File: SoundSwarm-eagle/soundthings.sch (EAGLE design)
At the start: 32 parts, among them Q2 MOSFET-NCHANNEL2N7000, Q4 MOSFET-NCHANNEL2N7000, Q5 MOSFET-PCHANNELFQP27P06

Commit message: v2 (to be tested)
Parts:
- added R13: 300, SparkFun-Passives:RESISTORAXIAL-0.3
- D1: value (none) -> 1N4001
- D3: value DIODE-ZENERPTH -> 1N5817; device SparkFun-DiscreteSemi:DIODE-ZENERPTH -> adafruit:SCHOTTKY-DIODEDO41
- Q1: value MOSFET-PCHANNELFQP27P06 -> IRLIB9343PbF
- Q2, Q4: value MOSFET-NCHANNEL2N7000 -> IRLB8721PBF; device SparkFun-DiscreteSemi:MOSFET-NCHANNEL2N7000 -> SparkFun-DiscreteSemi:MOSFET-NCHANNELFQP30N06L
- R8: value (none) -> 300
- U$2: value TP4057SOT-26-R -> TP4057
- renumbered D2 to LED, JP1-3V3 to 3V3, JP1-SOL to SOLENOID, JP2-ADXL to ADXL, JP2-BAT to BAT, Q5 to Q1
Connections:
- net N$10 renamed 5V
- net N$13 renamed GATE
- net N$17 renamed ADC
- net N$4 renamed GPIO16
- new net N$4: C1.-, Q1.D, Q4.D, R13.2
- net N$12: now also R13.1; no longer C1.-, Q1.S, Q4.D
- net VBAT: now also Q1.S; no longer Q1.D

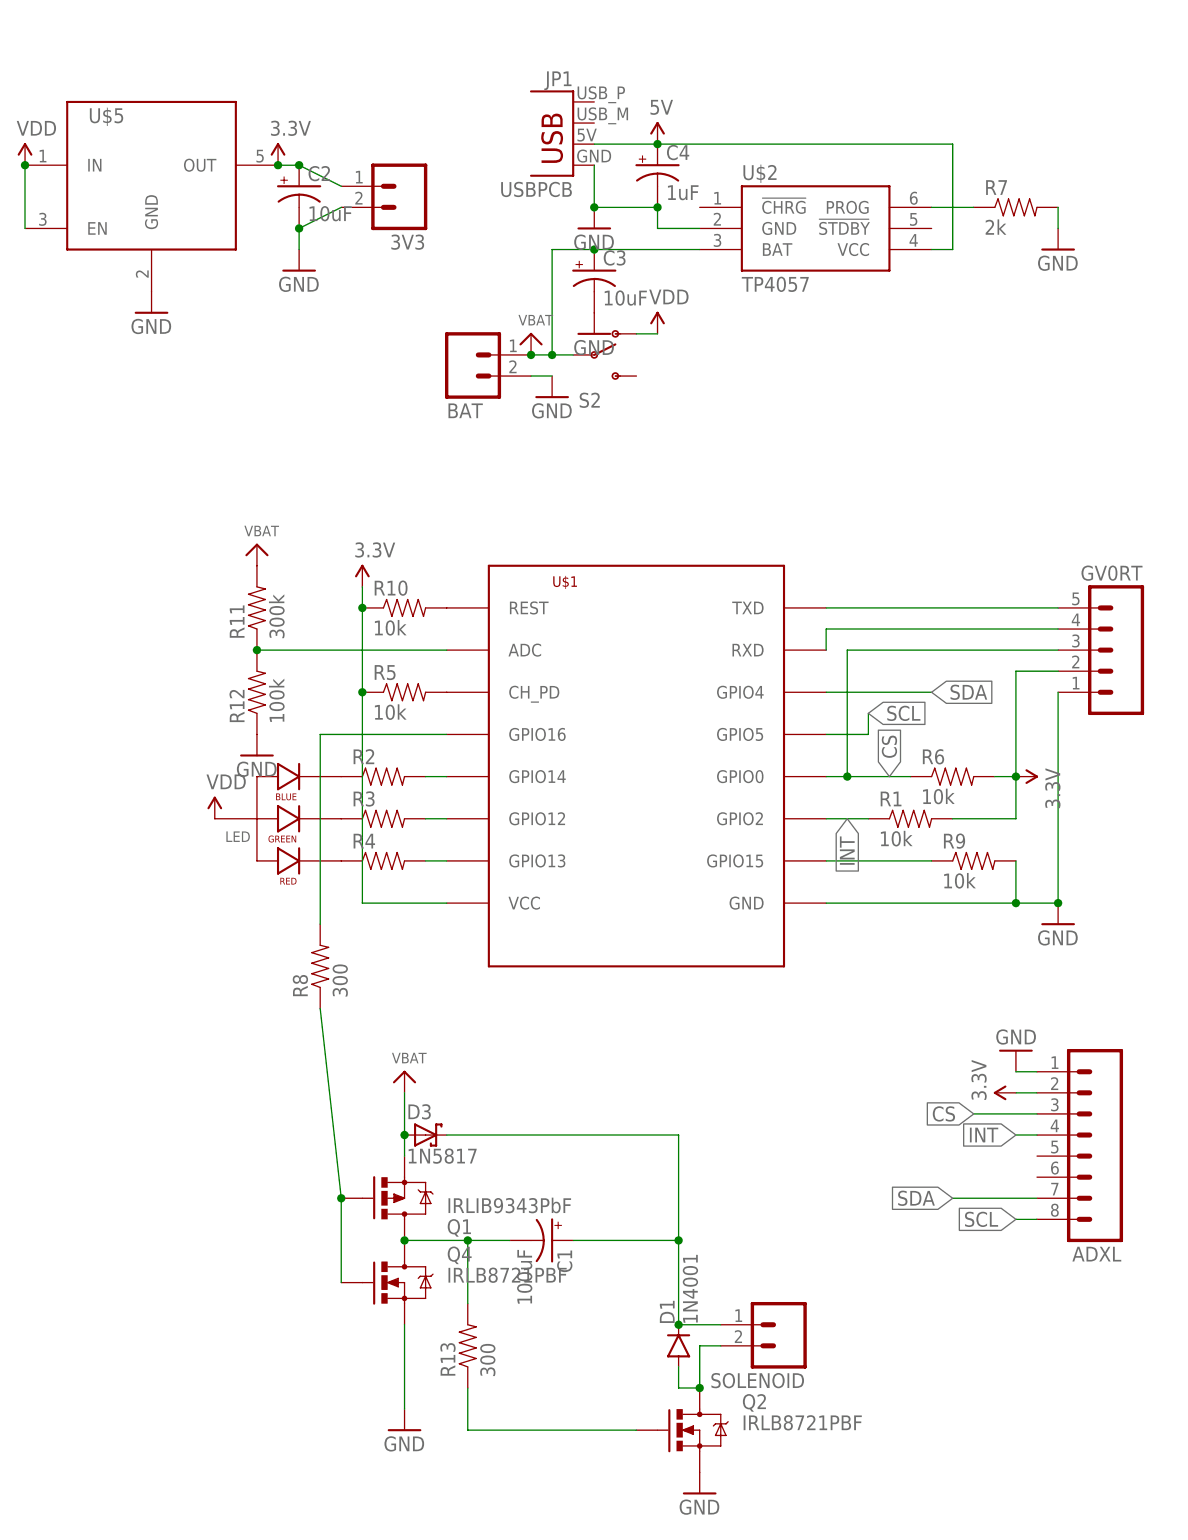
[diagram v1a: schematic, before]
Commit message: Update board with mounting holes
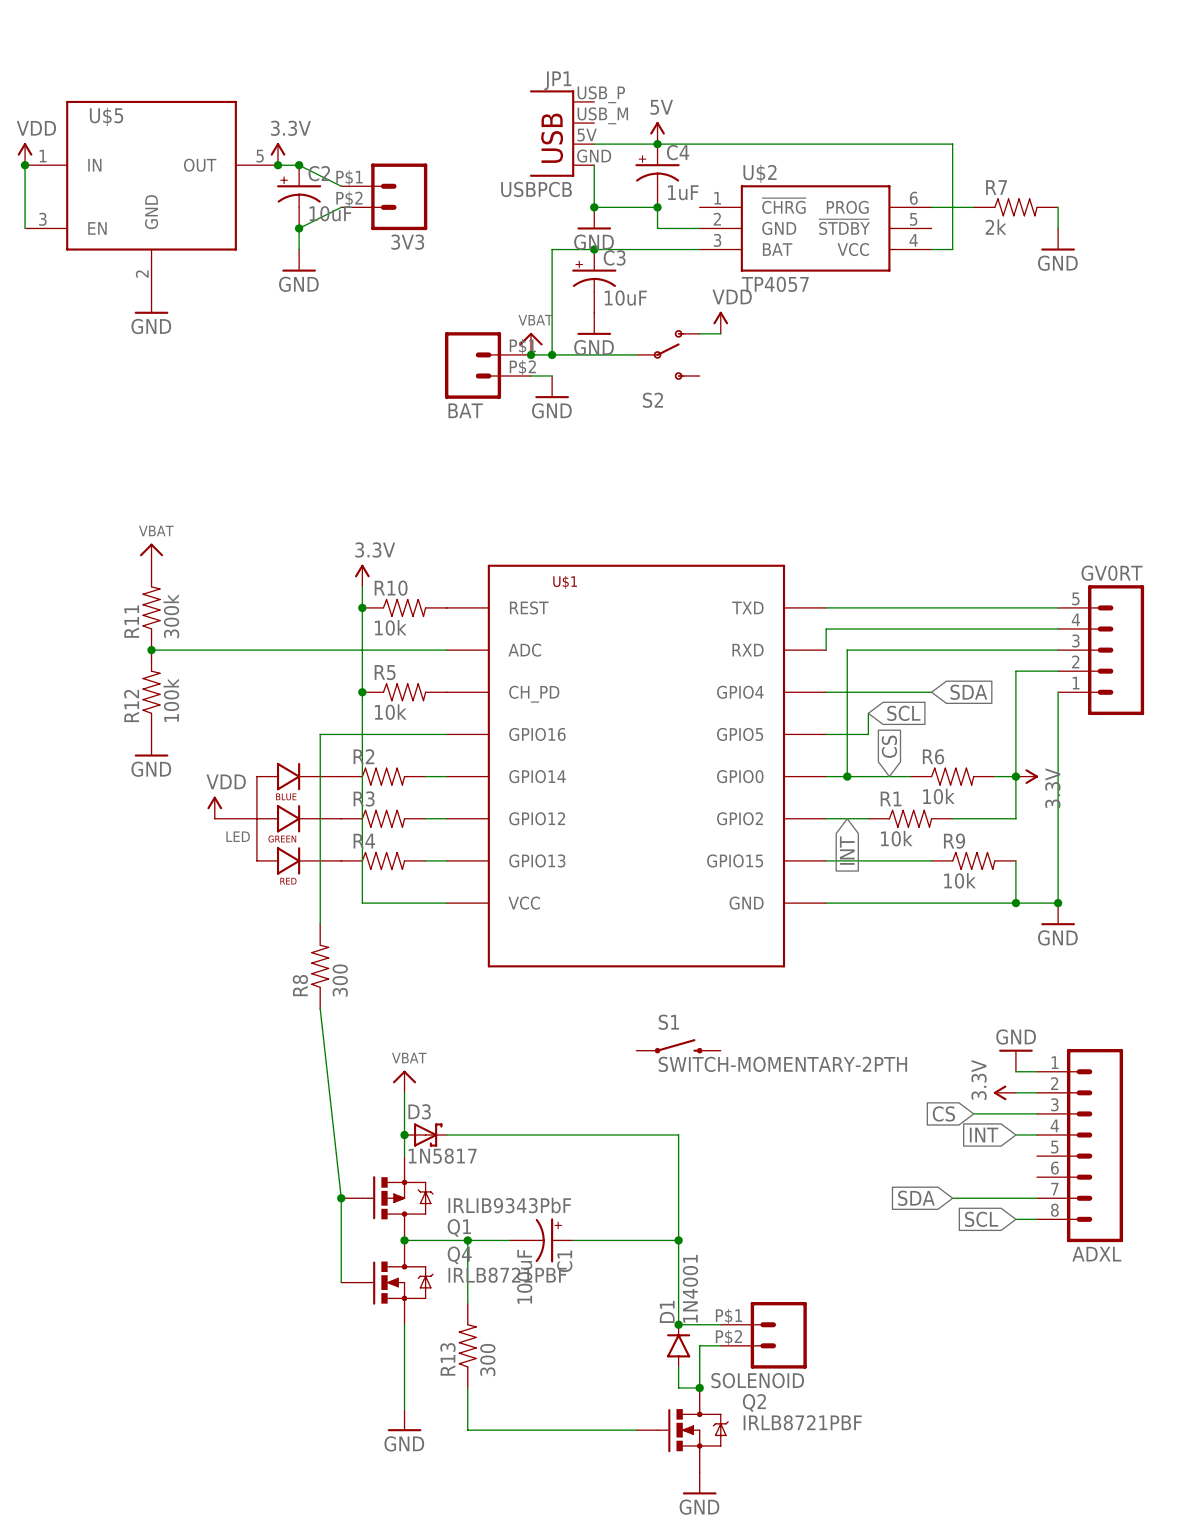
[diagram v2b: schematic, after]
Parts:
- added S1: SWITCH-MOMENTARY-2PTH, SparkFun-Electromechanical:SWITCH-MOMENTARY-2PTH
- 3V3, BAT, SOLENOID: device SparkFun-Connectors:M02JST-PTH-VERT -> SparkFun-Connectors:M02PTH2
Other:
- moved on the sheet: 3V3, BAT, R11, R12, S2, SOLENOID
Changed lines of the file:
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@@
 <part name="U$2" library="lio" deviceset="TP4057" device="SOT-26-R" value="TP4057"/>
 <part name="S2" library="lio" deviceset="SWITCH-SPDT" device="-1"/>
-<part name="SOLENOID" library="SparkFun-Connectors" deviceset="M02" device="JST-PTH-VERT"/>
-<part name="BAT" library="SparkFun-Connectors" deviceset="M02" device="JST-PTH-VERT"/>
+<part name="SOLENOID" library="SparkFun-Connectors" deviceset="M02" device="PTH2"/>
+<part name="BAT" library="SparkFun-Connectors" deviceset="M02" device="PTH2"/>
 <part name="D1" library="SparkFun-DiscreteSemi" deviceset="DIODE" device="1N4148" value="1N4001"/>
 <part name="C1" library="SparkFun-Capacitors" deviceset="100UF-25V-20%(PTH)" device="" value="100uF"/>
@@
 <part name="GND3" library="SparkFun-Aesthetics" deviceset="GND" device=""/>
 <part name="GND4" library="SparkFun-Aesthetics" deviceset="GND" device=""/>
-<part name="3V3" library="SparkFun-Connectors" deviceset="M02" device="JST-PTH-VERT"/>
+<part name="3V3" library="SparkFun-Connectors" deviceset="M02" device="PTH2"/>
 <part name="R5" library="SparkFun-Passives" deviceset="RESISTOR" device="AXIAL-0.3" value="10k"/>
 <part name="R6" library="SparkFun-Passives" deviceset="RESISTOR" device="AXIAL-0.3" value="10k"/>
@@
 <part name="R13" library="SparkFun-Passives" deviceset="RESISTOR" device="AXIAL-0.3" value="300"/>
 <part name="D3" library="adafruit" deviceset="SCHOTTKY-DIODE" device="DO41" value="1N5817"/>
+<part name="S1" library="SparkFun-Electromechanical" deviceset="SWITCH-MOMENTARY-2" device="PTH"/>
 </parts>
 <sheets>
@@
 <instance part="U$1" gate="G$1" x="60.96" y="93.98"/>
 <instance part="U$2" gate="G$1" x="83.82" y="165.1"/>
-<instance part="S2" gate="1" x="58.42" y="149.86"/>
+<instance part="S2" gate="1" x="66.04" y="149.86"/>
 <instance part="SOLENOID" gate="G$1" x="81.28" y="33.02" rot="R180"/>
 <instance part="BAT" gate="G$1" x="43.18" y="149.86" rot="MR180"/>
@@
 <instance part="GND5" gate="1" x="109.22" y="66.04" rot="R180"/>
 <instance part="SUPPLY6" gate="G$1" x="109.22" y="60.96" rot="R90"/>
-<instance part="SUPPLY7" gate="VDD" x="66.04" y="152.4"/>
+<instance part="SUPPLY7" gate="VDD" x="73.66" y="152.4"/>
 <instance part="SUPPLY8" gate="VDD" x="-10.16" y="172.72"/>
 <instance part="SUPPLY9" gate="VDD" x="12.7" y="93.98"/>
@@
 <instance part="GND7" gate="1" x="58.42" y="152.4"/>
 <instance part="C4" gate="G$1" x="66.04" y="172.72"/>
-<instance part="R11" gate="G$1" x="17.78" y="119.38" rot="R90"/>
-<instance part="R12" gate="G$1" x="17.78" y="109.22" rot="R90"/>
-<instance part="U$6" gate="G$1" x="17.78" y="127"/>
-<instance part="GND11" gate="1" x="17.78" y="101.6"/>
+<instance part="R11" gate="G$1" x="5.08" y="119.38" rot="R90"/>
+<instance part="R12" gate="G$1" x="5.08" y="109.22" rot="R90"/>
+<instance part="U$6" gate="G$1" x="5.08" y="127"/>
+<instance part="GND11" gate="1" x="5.08" y="101.6"/>
 <instance part="SUPPLY1" gate="G$1" x="66.04" y="175.26"/>
 <instance part="Q1" gate="G$1" x="35.56" y="48.26" rot="MR180"/>
 <instance part="R13" gate="G$1" x="43.18" y="30.48" rot="R90"/>
 <instance part="D3" gate="G$1" x="38.1" y="55.88"/>
+<instance part="S1" gate="G$1" x="68.58" y="66.04"/>
 </instances>
 <busses>
@@
 <wire x1="50.8" y1="149.86" x2="53.34" y2="149.86" width="0.1524" layer="91"/>
 <pinref part="U$2" gate="G$1" pin="BAT"/>
-<wire x1="53.34" y1="149.86" x2="55.88" y2="149.86" width="0.1524" layer="91"/>
+<wire x1="53.34" y1="149.86" x2="63.5" y2="149.86" width="0.1524" layer="91"/>
 <wire x1="71.12" y1="162.56" x2="58.42" y2="162.56" width="0.1524" layer="91"/>
 <wire x1="58.42" y1="162.56" x2="53.34" y2="162.56" width="0.1524" layer="91"/>
@@
 <pinref part="S2" gate="1" pin="O"/>
 <pinref part="SUPPLY7" gate="VDD" pin="VDD"/>
-<wire x1="66.04" y1="152.4" x2="63.5" y2="152.4" width="0.1524" layer="91"/>
+<wire x1="73.66" y1="152.4" x2="71.12" y2="152.4" width="0.1524" layer="91"/>
 </segment>
 <segment>
@@
 <pinref part="R12" gate="G$1" pin="2"/>
 <pinref part="U$1" gate="G$1" pin="ADC"/>
-<wire x1="17.78" y1="114.3" x2="40.64" y2="114.3" width="0.1524" layer="91"/>
-<junction x="17.78" y="114.3"/>
-</segment>
-</net>
+<wire x1="5.08" y1="114.3" x2="40.64" y2="114.3" width="0.1524" layer="91"/>
+<junction x="5.08" y="114.3"/>
+</segment>
+</net>

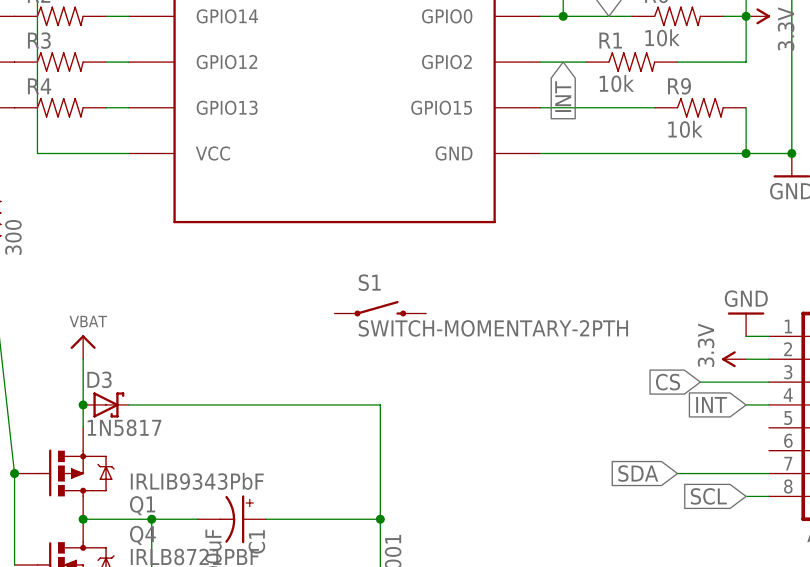
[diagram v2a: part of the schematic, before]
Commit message: removed names and added values
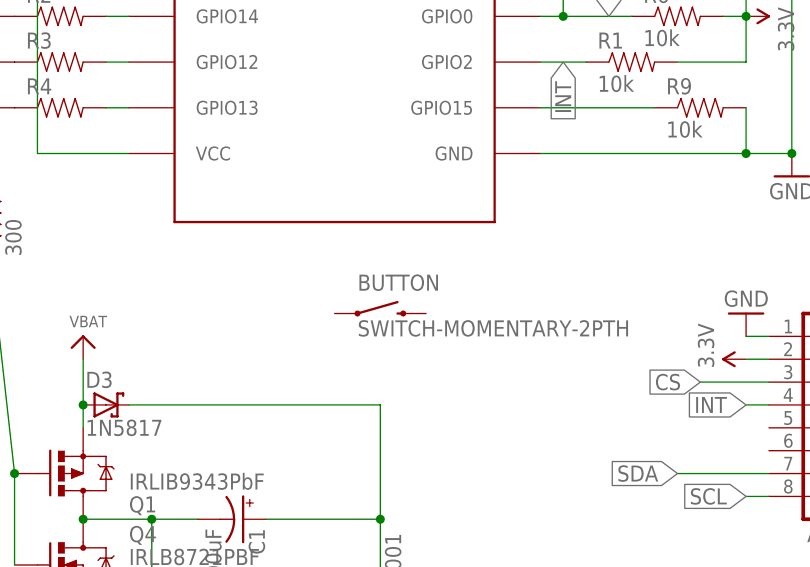
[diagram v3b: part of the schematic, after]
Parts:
- renumbered S1 to BUTTON
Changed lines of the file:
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@@
 <?xml version="1.0" encoding="utf-8"?>
 <!DOCTYPE eagle SYSTEM "eagle.dtd">
-<eagle version="7.7.0">
+<eagle version="8.0.2">
 <drawing>
 <settings>
@@
 <grid distance="0.1" unitdist="inch" unit="inch" style="lines" multiple="1" display="no" altdistance="0.01" altunitdist="inch" altunit="inch"/>
 <layers>
-<layer number="1" name="Top" color="4" fill="1" visible="yes" active="no"/>
-<layer number="16" name="Bottom" color="1" fill="1" visible="yes" active="no"/>
-<layer number="17" name="Pads" color="2" fill="1" visible="yes" active="no"/>
-<layer number="18" name="Vias" color="2" fill="1" visible="yes" active="no"/>
-<layer number="19" name="Unrouted" color="6" fill="1" visible="yes" active="no"/>
-<layer number="20" name="Dimension" color="15" fill="1" visible="yes" active="no"/>
-<layer number="21" name="tPlace" color="7" fill="1" visible="yes" active="no"/>
-<layer number="22" name="bPlace" color="7" fill="1" visible="yes" active="no"/>
-<layer number="23" name="tOrigins" color="15" fill="1" visible="yes" active="no"/>
-<layer number="24" name="bOrigins" color="15" fill="1" visible="yes" active="no"/>
-<layer number="25" name="tNames" color="7" fill="1" visible="yes" active="no"/>
-<layer number="26" name="bNames" color="7" fill="1" visible="yes" active="no"/>
-<layer number="27" name="tValues" color="7" fill="1" visible="yes" active="no"/>
-<layer number="28" name="bValues" color="7" fill="1" visible="yes" active="no"/>
+<layer number="1" name="Top" color="4" fill="1" visible="no" active="no"/>
+<layer number="16" name="Bottom" color="1" fill="1" visible="no" active="no"/>
+<layer number="17" name="Pads" color="2" fill="1" visible="no" active="no"/>
+<layer number="18" name="Vias" color="2" fill="1" visible="no" active="no"/>
+<layer number="19" name="Unrouted" color="6" fill="1" visible="no" active="no"/>
+<layer number="20" name="Dimension" color="15" fill="1" visible="no" active="no"/>
+<layer number="21" name="tPlace" color="7" fill="1" visible="no" active="no"/>
+<layer number="22" name="bPlace" color="7" fill="1" visible="no" active="no"/>
+<layer number="23" name="tOrigins" color="15" fill="1" visible="no" active="no"/>
+<layer number="24" name="bOrigins" color="15" fill="1" visible="no" active="no"/>
+<layer number="25" name="tNames" color="7" fill="1" visible="no" active="no"/>
+<layer number="26" name="bNames" color="7" fill="1" visible="no" active="no"/>
+<layer number="27" name="tValues" color="7" fill="1" visible="no" active="no"/>
+<layer number="28" name="bValues" color="7" fill="1" visible="no" active="no"/>
 <layer number="29" name="tStop" color="7" fill="3" visible="no" active="no"/>
 <layer number="30" name="bStop" color="7" fill="6" visible="no" active="no"/>
@@
 <layer number="35" name="tGlue" color="7" fill="4" visible="no" active="no"/>
 <layer number="36" name="bGlue" color="7" fill="5" visible="no" active="no"/>
-<layer number="37" name="tTest" color="7" fill="1" visible="yes" active="no"/>
-<layer number="38" name="bTest" color="7" fill="1" visible="yes" active="no"/>
+<layer number="37" name="tTest" color="7" fill="1" visible="no" active="no"/>
+<layer number="38" name="bTest" color="7" fill="1" visible="no" active="no"/>
 <layer number="39" name="tKeepout" color="4" fill="11" visible="no" active="no"/>
 <layer number="40" name="bKeepout" color="1" fill="11" visible="no" active="no"/>
@@
 <layer number="44" name="Drills" color="7" fill="1" visible="no" active="no"/>
 <layer number="45" name="Holes" color="7" fill="1" visible="no" active="no"/>
-<layer number="46" name="Milling" color="3" fill="1" visible="yes" active="no"/>
-<layer number="47" name="Measures" color="7" fill="1" visible="yes" active="no"/>
-<layer number="48" name="Document" color="7" fill="1" visible="yes" active="no"/>
-<layer number="49" name="Reference" color="7" fill="1" visible="yes" active="no"/>
-<layer number="50" name="dxf" color="7" fill="1" visible="yes" active="no"/>
-<layer number="51" name="tDocu" color="7" fill="1" visible="yes" active="no"/>
-<layer number="52" name="bDocu" color="7" fill="1" visible="yes" active="no"/>
-<layer number="53" name="tGND_GNDA" color="7" fill="9" visible="yes" active="no"/>
-<layer number="54" name="bGND_GNDA" color="1" fill="9" visible="yes" active="no"/>
-<layer number="56" name="wert" color="7" fill="1" visible="yes" active="no"/>
-<layer number="57" name="tCAD" color="7" fill="1" visible="yes" active="no"/>
-<layer number="59" name="tCarbon" color="7" fill="1" visible="yes" active="no"/>
-<layer number="60" name="bCarbon" color="7" fill="1" visible="yes" active="no"/>
+<layer number="46" name="Milling" color="3" fill="1" visible="no" active="no"/>
+<layer number="47" name="Measures" color="7" fill="1" visible="no" active="no"/>
+<layer number="48" name="Document" color="7" fill="1" visible="no" active="no"/>
+<layer number="49" name="Reference" color="7" fill="1" visible="no" active="no"/>
+<layer number="50" name="dxf" color="7" fill="1" visible="no" active="no"/>
+<layer number="51" name="tDocu" color="7" fill="1" visible="no" active="no"/>
+<layer number="52" name="bDocu" color="7" fill="1" visible="no" active="no"/>
+<layer number="53" name="tGND_GNDA" color="7" fill="9" visible="no" active="no"/>
+<layer number="54" name="bGND_GNDA" color="1" fill="9" visible="no" active="no"/>
+<layer number="56" name="wert" color="7" fill="1" visible="no" active="no"/>
+<layer number="57" name="tCAD" color="7" fill="1" visible="no" active="no"/>
+<layer number="59" name="tCarbon" color="7" fill="1" visible="no" active="no"/>
+<layer number="60" name="bCarbon" color="7" fill="1" visible="no" active="no"/>
 <layer number="90" name="Modules" color="5" fill="1" visible="yes" active="yes"/>
 <layer number="91" name="Nets" color="2" fill="1" visible="yes" active="yes"/>
@@
 <part name="R13" library="SparkFun-Passives" deviceset="RESISTOR" device="AXIAL-0.3" value="300"/>
 <part name="D3" library="adafruit" deviceset="SCHOTTKY-DIODE" device="DO41" value="1N5817"/>
-<part name="S1" library="SparkFun-Electromechanical" deviceset="SWITCH-MOMENTARY-2" device="PTH"/>
+<part name="BUTTON" library="SparkFun-Electromechanical" deviceset="SWITCH-MOMENTARY-2" device="PTH"/>
 </parts>
 <sheets>
@@
 <instance part="R13" gate="G$1" x="43.18" y="30.48" rot="R90"/>
 <instance part="D3" gate="G$1" x="38.1" y="55.88"/>
-<instance part="S1" gate="G$1" x="68.58" y="66.04"/>
+<instance part="BUTTON" gate="G$1" x="68.58" y="66.04"/>
 </instances>
 <busses>
